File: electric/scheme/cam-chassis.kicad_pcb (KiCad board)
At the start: 2 copper layers, 51.5 x 28.5 mm, 48 parts, among them IC1 ATMEGA8-AI, K1 pyro, P1 TST, P2 TST, P3 TST, P4 TST, P5 TST, P6 TST, P7 servo, Q3 bc857, Q4 bc847, Q5 irlml2244, Q6 NPN, Q7 irlml2244, U1 MINI-USB-B-4-bases, Y1 Crystal

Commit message: a
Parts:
- removed C5, C6: 100n, Capacitors_SMD:C_0805_HandSoldering
- removed R18: 100k, Resistors_SMD:R_0805_HandSoldering
- moved U1 42.3 mm to (107.9, 83.5), turned to 270 degrees
- moved Y1 26.7 mm to (118.3, 96.5), turned to 270 degrees
- moved R17 16.6 mm to (120.1, 84.1), turned to 0 degrees
- moved R11 16.1 mm to (118.8, 81.8)
- moved Q7 13.2 mm to (123.9, 89.1)
- moved Q6 13.1 mm to (121.1, 87.4)
- moved R15 12.4 mm to (123.9, 83.3), turned to 90 degrees
- moved C7 10.0 mm to (131.0, 95.5), turned to 180 degrees
- moved R20 9.85 mm to (141.7, 101.8)
- moved D6 6.87 mm to (146.3, 96.2)
- moved C3 6.80 mm to (107.4, 111.0), turned to 0 degrees
- moved D4 6.42 mm to (145.0, 106.7)
- moved K1 5.53 mm to (140.9, 87.6)
- moved Q3 5.00 mm to (125.2, 102.1)
- moved Q5 4.76 mm to (125.7, 105.9), turned to 90 degrees
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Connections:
- U1 pad 4: Net-(R18-Pad1) -> GND
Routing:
- net GND: track 239.9 -> 58.1 mm, vias 3 -> 0
- net VCC: track 135.7 -> 27.4 mm, vias 5 -> 0
- net /pyro-sen: track 57.7 -> 0.00 mm, vias 1 -> 0
- net (no net): track 0.00 -> 55.5 mm
- net /servo1: track 32.5 -> 0.00 mm, vias 2 -> 0
- net /servo2: track 25.4 -> 0.00 mm, vias 2 -> 0
- net /gate: track 25.3 -> 0.00 mm
- net /servo-vcc: track 21.0 -> 0.00 mm
- net /led: track 14.5 -> 0.00 mm
- net /src: track 12.6 -> 0.00 mm
- net /d-: track 13.0 -> 3.13 mm
- net /xtal2: track 8.35 -> 0.00 mm
- net /rst: track 37.4 -> 29.5 mm, vias 1 -> 2
- net Net-(P7-Pad5): track 7.84 -> 0.00 mm
- net /xtal1: track 7.34 -> 0.00 mm
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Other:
- board size 51.5 x 28.5 mm -> 51.5 x 32.6 mm

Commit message: a
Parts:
- moved R8 1.11 mm to (101.2, 108.1)
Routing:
- net GND: track 58.1 -> 225.5 mm, vias 0 -> 3
- net VCC: track 27.4 -> 158.8 mm, vias 0 -> 1
- net /pyro-sen: track 0.00 -> 84.6 mm
- net (no net): track 55.5 -> 0.00 mm
- net /servo1: track 0.00 -> 40.2 mm
- net /led: track 0.00 -> 33.7 mm, vias 0 -> 2
- net /gate: track 0.00 -> 30.3 mm, vias 0 -> 2
- net /servo2: track 0.00 -> 25.6 mm
- net /servo-vcc: track 0.00 -> 20.6 mm
- net /xtal2: track 0.00 -> 13.3 mm
- net /src: track 0.00 -> 11.1 mm
- net /xtal1: track 0.00 -> 10.5 mm
- net /d-: track 3.13 -> 12.6 mm
- net Net-(D1-Pad1): track 0.00 -> 4.16 mm
- net /dbg-led: track 0.00 -> 2.78 mm
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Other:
- board size 51.5 x 32.6 mm -> 51.5 x 34.6 mm

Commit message: Prepared SVG.
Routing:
- net GND: track 225.5 -> 244.2 mm
- net Net-(Q4-Pad3): track 0.00 -> 1.90 mm
- net /gate: track 30.3 -> 31.9 mm
- net VCC: track 158.8 -> 160.0 mm

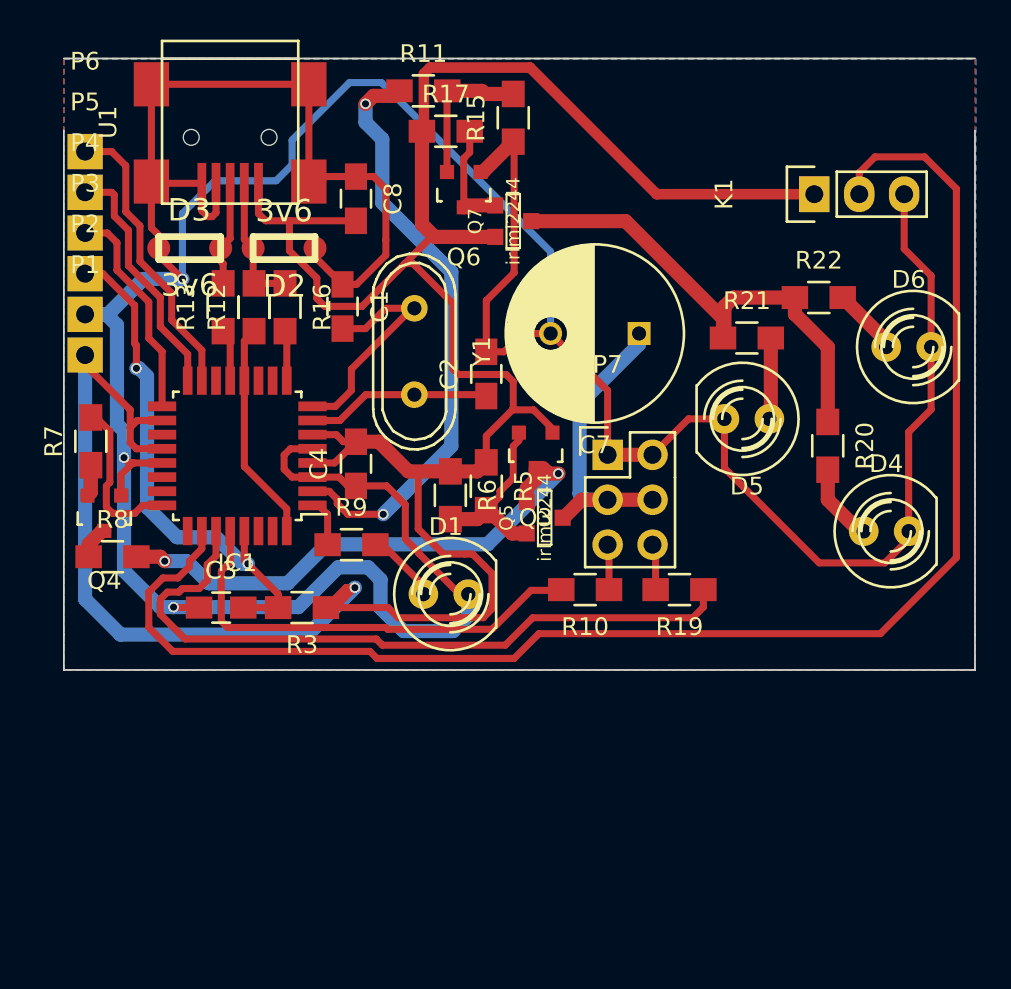
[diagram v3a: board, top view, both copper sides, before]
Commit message: Made LEDs power also limited.
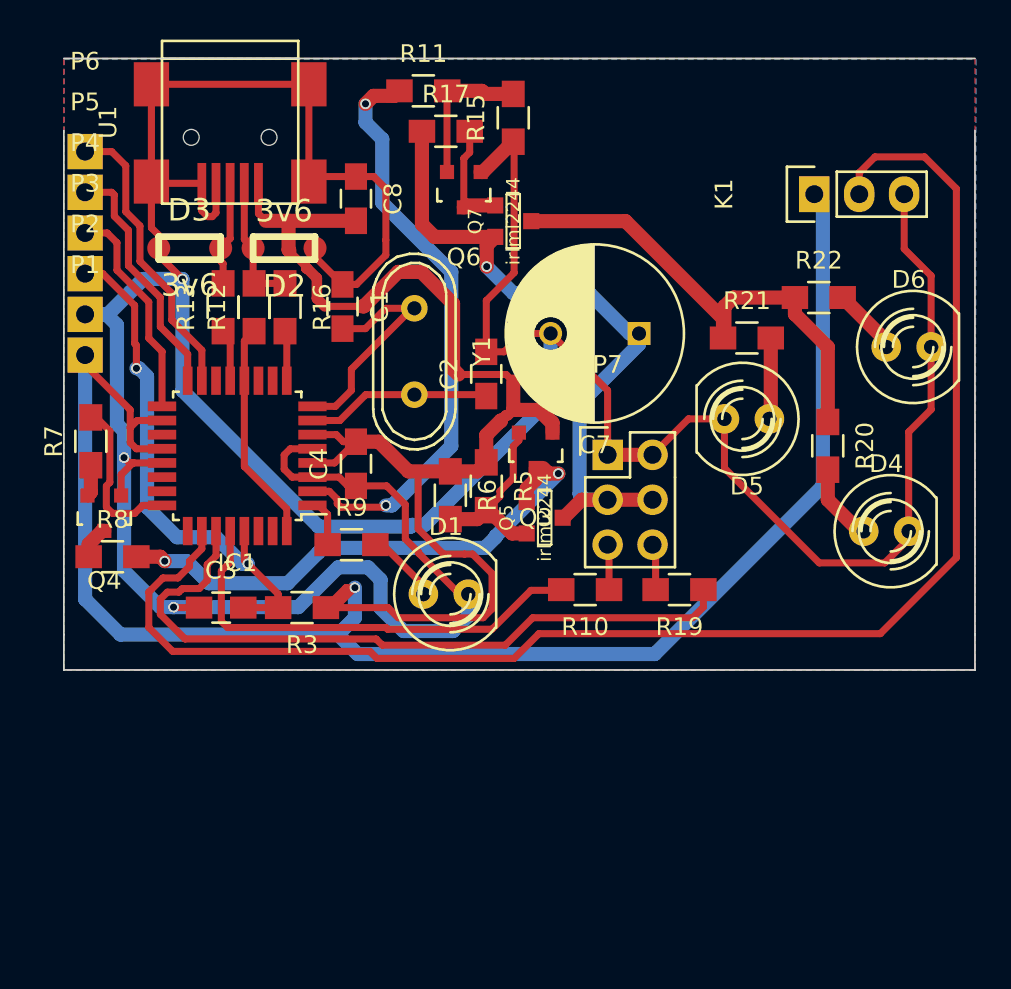
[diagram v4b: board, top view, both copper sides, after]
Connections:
- Q7 pad S: VCC -> /servo-vcc
- R17 pad 1: VCC -> /servo-vcc
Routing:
- net VCC: track 160.0 -> 187.4 mm
- net /servo-vcc: track 20.6 -> 42.7 mm, vias 0 -> 1

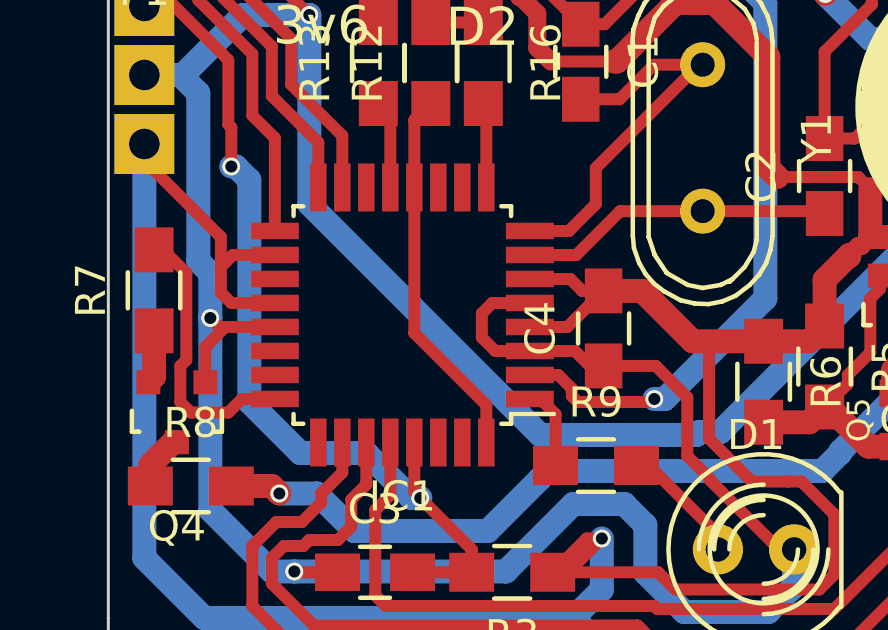
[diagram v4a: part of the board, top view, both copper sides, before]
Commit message: INT0 must be connected to D+ - not D- (!!!)
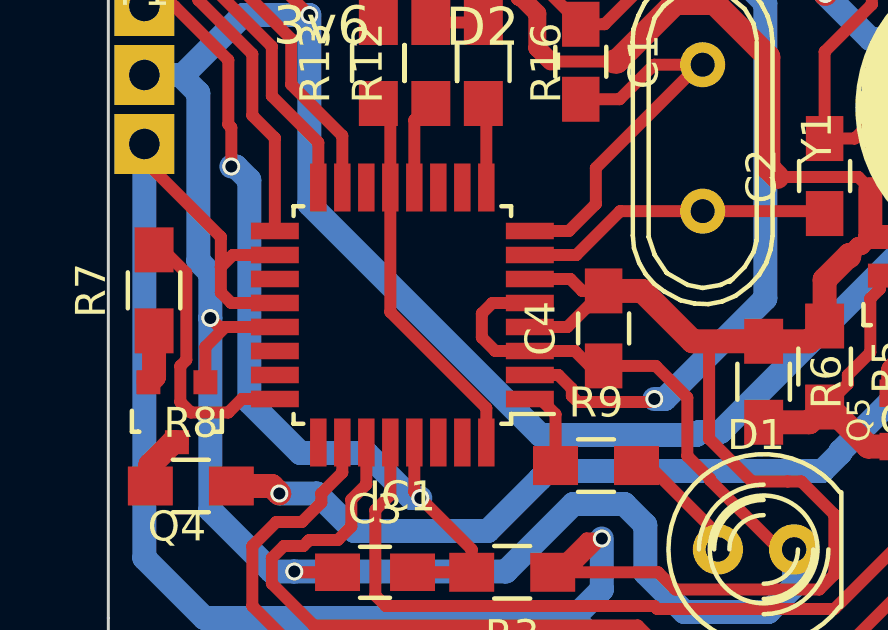
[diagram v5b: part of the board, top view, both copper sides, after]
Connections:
- IC1 pad 32: /d- -> /d+
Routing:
- net /d+: track 3.58 -> 13.4 mm
- net /d-: track 12.6 -> 3.13 mm
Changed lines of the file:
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@@
     (links 89)
     (no_connects 0)
-    (area 96.67281 78.468999 150.100001 114.999)
+    (area 98.449999 79.885999 150.050001 114.550001)
     (thickness 1.6)
     (drawings 9)
@@
   )
   (setup
-    (last_trace_width 0.8)
+    (last_trace_width 0.4)
     (user_trace_width 0.4)
     (user_trace_width 0.6)
@@
     (pad 31 smd rect (at -2 -4.25 270) (size 1.6 0.55) (layers F.Cu F.Paste F.Mask))
     (pad 32 smd rect (at -2.8 -4.25 270) (size 1.6 0.55) (layers F.Cu F.Paste F.Mask)
-      (net 9 /d-))
+      (net 8 /d+))
     (model Housings_QFP.3dshapes/TQFP-32_7x7mm_Pitch0.8mm.wrl
       (at (xyz 0 0 0))
@@
   (segment (start 117.186 82.05) (end 117.47 81.766) (width 0.8) (layer F.Cu) (net 7))
   (segment (start 117.186 82.05) (end 117.47 81.766) (width 0.4) (layer F.Cu) (net 7))
+  (segment (start 111.1 106.65) (end 111.1 105.5) (width 0.4) (layer F.Cu) (net 8))
+  (segment (start 107.9 102.3) (end 107.9 98.15) (width 0.4) (layer F.Cu) (net 8))
+  (segment (start 111.1 105.5) (end 107.9 102.3) (width 0.4) (layer F.Cu) (net 8))
   (segment (start 107.9 98.15) (end 107.9 95.75) (width 0.4) (layer F.Cu) (net 8))
   (segment (start 107.9 95.75) (end 107.5 95.35) (width 0.4) (layer F.Cu) (net 8))
   (segment (start 107.5 94.95) (end 107.5 95) (width 0.4) (layer F.Cu) (net 8))
   (segment (start 107.5 95) (end 107.9 95.4) (width 0.4) (layer F.Cu) (net 8))
-  (segment (start 111.1 106.65) (end 111.1 105.4) (width 0.4) (layer F.Cu) (net 9))
-  (segment (start 108.7 103) (end 108.7 98.15) (width 0.4) (layer F.Cu) (net 9))
-  (segment (start 111.1 105.4) (end 108.7 103) (width 0.4) (layer F.Cu) (net 9))
   (segment (start 108.7 98.15) (end 108.7 95.9) (width 0.4) (layer F.Cu) (net 9))
   (segment (start 108.7 95.9) (end 109.25 95.35) (width 0.4) (layer F.Cu) (net 9))
